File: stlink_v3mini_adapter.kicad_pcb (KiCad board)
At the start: 2 copper layers, 56.2 x 37 mm, 53 parts, among them J1 Conn_02x07_Odd_Even, J3 Conn_01x05_Pin, SW1 RST, U3 TLV71333PDBV

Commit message: 1.2.1: actually cut RX instead of TX..
Signed-off-by: Guillaume Revaillot <guillaume.revaillot@wirestone.io>
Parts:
- removed kibuzzard-6499595A: G***, kibuzzard-6499595A
- removed kibuzzard-6723780F: G***, kibuzzard-6723780F
- added kibuzzard-67449540: G***, kibuzzard-67449540, B.Cu at (101.5, 75.5)
- added kibuzzard-674495BA: G***, kibuzzard-674495BA, F.Cu at (79.5, 86.0)
- moved D7 1.65 mm to (65.3, 80.3)
- moved D8 1.40 mm to (65.3, 78.7), turned to 180 degrees
- turned JP2 to 90 degrees
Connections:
- JP1 pad 2: /TXD -> /RXD
- JP2 pad 1: /TXD -> Net-(JP1-A)
- JP2 pad 2: Net-(JP1-A) -> /RXD
- R10 pad 1: Net-(JP1-A) -> /TXD
- R9 pad 1: /RXD -> Net-(JP1-A)
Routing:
- net /TXD: track 18.3 -> 13.0 mm
- net /RXD: track 17.6 -> 22.6 mm
- net GND: track 20.5 -> 22.5 mm, vias 73 -> 75

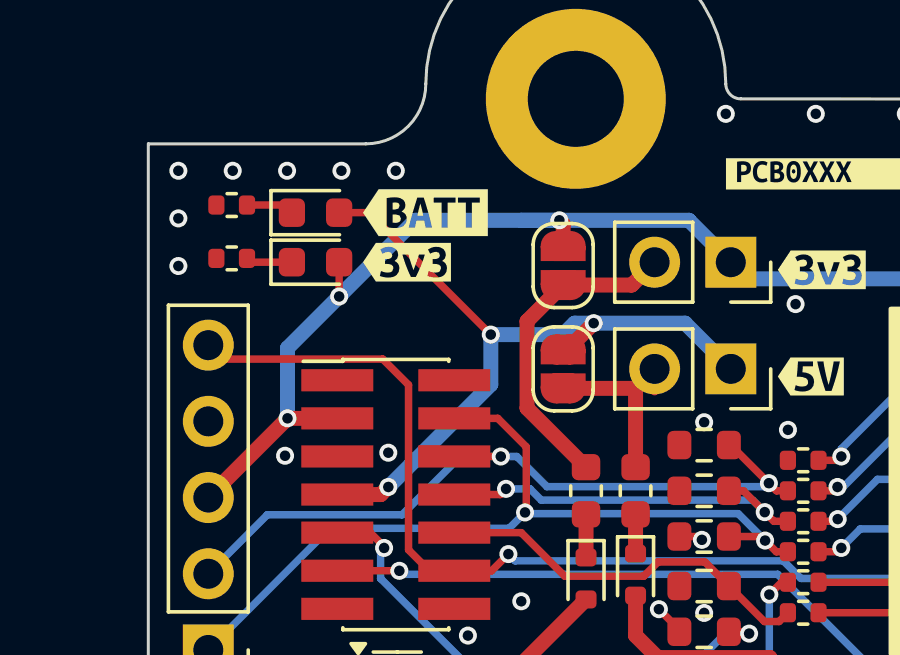
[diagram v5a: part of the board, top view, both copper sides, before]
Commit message: swap leds for 5v/3v3
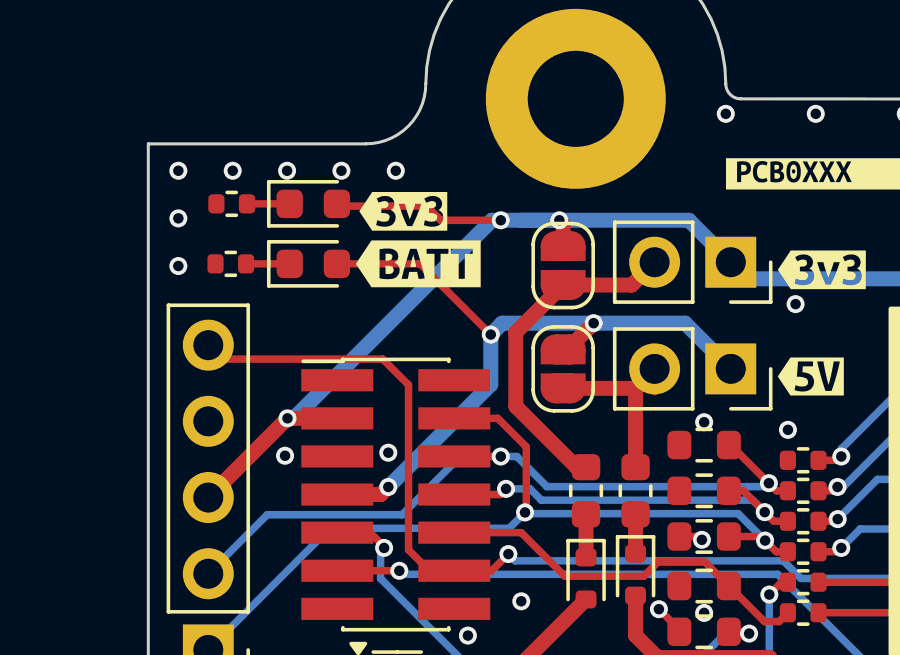
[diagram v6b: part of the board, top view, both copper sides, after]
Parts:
- moved R2 1.96 mm to (49.5, 68.0)
- moved D1 1.95 mm to (52.2, 66.0)
- moved R1 1.82 mm to (49.5, 66.0)
- moved kibuzzard-66EBEE9F 1.72 mm to (55.8, 68.0)
- moved D2 1.71 mm to (52.2, 68.0)
- moved kibuzzard-63D24BD9 1.70 mm to (55.2, 66.2)
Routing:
- net +3.3V: track 65.5 -> 68.7 mm
- net +BATT: track 25.2 -> 24.6 mm
